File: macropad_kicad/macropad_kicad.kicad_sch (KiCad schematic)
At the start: 34 parts, among them J1 OLED_128x64, SW1 RotaryEncoder_Switch, SW2 RotaryEncoder_Switch, U1 MOUDLE-SEEEDUINO-XIAO

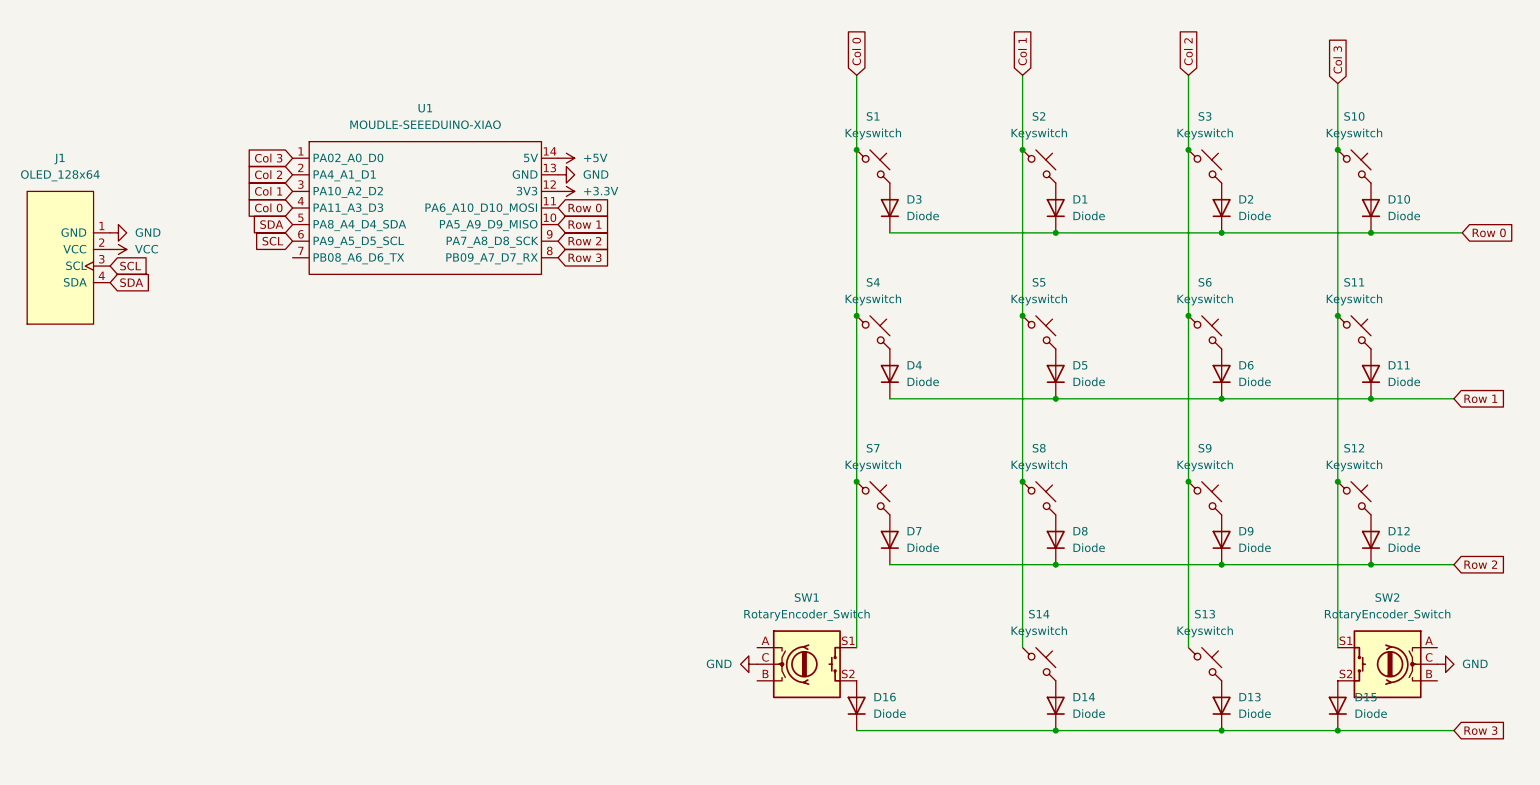
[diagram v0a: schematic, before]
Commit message: Add schematic for matrix and OLED display integration Re-Implemented schematic as there in not enough pins
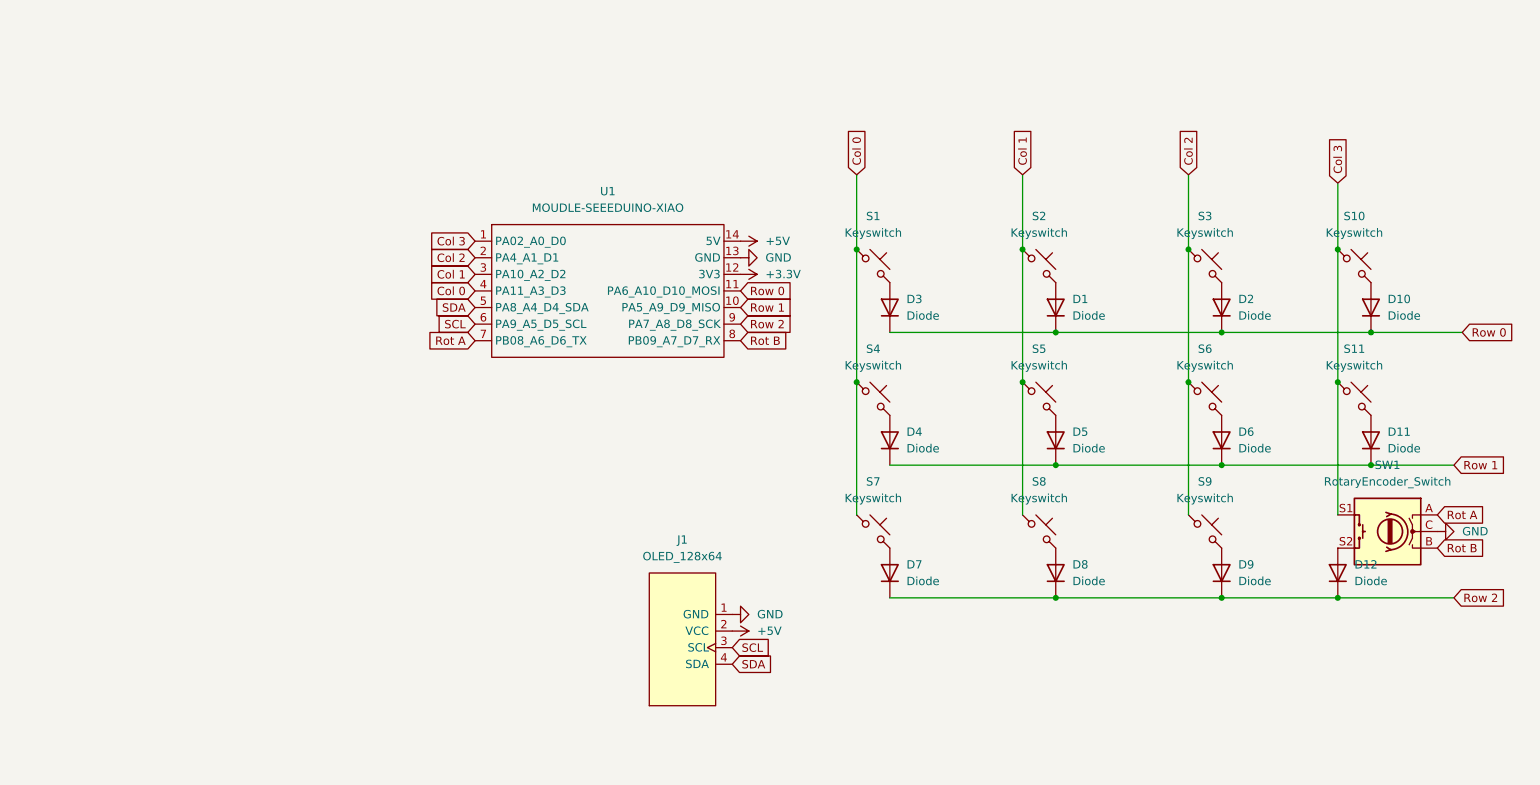
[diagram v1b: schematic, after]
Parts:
- removed D13, D14, D15, D16: Diode, symbol ScottoKeebs:Placeholder_Diode
- removed S12, S13, S14: Keyswitch, symbol ScottoKeebs:Placeholder_Keyswitch
- removed SW2: RotaryEncoder_Switch, symbol Device:RotaryEncoder_Switch
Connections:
- net Row 3 is gone; now on net Rot B: U1.8 (PB09_A7_D7_RX)
- net VCC is gone; now on net +5V: J1.2 (VCC)
- net Col 0: no longer SW1.S1
- net Col 3: now also SW1.S1
- net at D12.2 (A): now also SW1.S2
- net Rot A: now reaches U1.7 (PB08_A6_D6_TX)
- net Rot A: now also SW1.A
- net Rot B: now reaches SW1.B
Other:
- moved on the sheet: D1, D10, D11, D2, D3, D4, D5, D6, D7, D8, D9, J1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

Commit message: Update footprint properties and library URI in schematic files created pcb with footprints
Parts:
- D1, D10, D11, D12, D2, D3, D4, D5, D6, D7, D8, D9: footprint (none) -> ScottoKeebs_Components:Diode_DO-35
- S1, S10, S11, S2, S3, S4, S5, S6, S7, S8, S9: footprint (none) -> Button_Switch_Keyboard:SW_Cherry_MX_1.00u_PCB
- SW1: footprint (none) -> Rotary_Encoder:RotaryEncoder_Alps_EC11E-Switch_Vertical_H20mm
- U1: footprint (none) -> XIAO_PCB:MOUDLE14P-2.54-21X17.8MM
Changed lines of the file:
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@@
 			)
 		)
-		(property "Footprint" ""
+		(property "Footprint" "Button_Switch_Keyboard:SW_Cherry_MX_1.00u_PCB"
 			(at 180.34 121.92 0)
 			(effects
@@
 			)
 		)
-		(property "Footprint" ""
+		(property "Footprint" "ScottoKeebs_Components:Diode_DO-35"
 			(at 233.68 87.63 0)
 			(effects
@@
 			)
 		)
-		(property "Footprint" ""
+		(property "Footprint" "Button_Switch_Keyboard:SW_Cherry_MX_1.00u_PCB"
 			(at 231.14 81.28 0)
 			(effects
@@
 			)
 		)
-		(property "Footprint" ""
+		(property "Footprint" "Button_Switch_Keyboard:SW_Cherry_MX_1.00u_PCB"
 			(at 205.74 121.92 0)
 			(effects
@@
 			)
 		)
-		(property "Footprint" ""
+		(property "Footprint" "ScottoKeebs_Components:Diode_DO-35"
 			(at 208.28 87.63 0)
 			(effects
@@
 			)
 		)
-		(property "Footprint" ""
+		(property "Footprint" "ScottoKeebs_Components:Diode_DO-35"
 			(at 233.68 128.27 0)
 			(effects
@@
 			)
 		)
-		(property "Footprint" ""
+		(property "Footprint" "Button_Switch_Keyboard:SW_Cherry_MX_1.00u_PCB"
 			(at 180.34 81.28 0)
 			(effects
@@
 			)
 		)
-		(property "Footprint" ""
+		(property "Footprint" "ScottoKeebs_Components:Diode_DO-35"
 			(at 233.68 107.95 0)
 			(effects
@@
 			)
 		)
-		(property "Footprint" ""
+		(property "Footprint" "Button_Switch_Keyboard:SW_Cherry_MX_1.00u_PCB"
 			(at 205.74 101.6 0)
 			(effects
@@
 			)
 		)
-		(property "Footprint" ""
+		(property "Footprint" "ScottoKeebs_Components:Diode_DO-35"
 			(at 208.28 107.95 0)
 			(effects
@@
 			)
 		)
-		(property "Footprint" ""
+		(property "Footprint" "ScottoKeebs_Components:Diode_DO-35"
 			(at 208.28 128.27 0)
 			(effects
@@
 			)
 		)
-		(property "Footprint" ""
+		(property "Footprint" "ScottoKeebs_Components:Diode_DO-35"
 			(at 256.54 87.63 0)
 			(effects
@@
 			)
 		)
-		(property "Footprint" ""
+		(property "Footprint" "XIAO_PCB:MOUDLE14P-2.54-21X17.8MM"
 			(at 121.92 82.55 0)
 			(effects
@@
 			)
 		)
-		(property "Footprint" ""
+		(property "Footprint" "Button_Switch_Keyboard:SW_Cherry_MX_1.00u_PCB"
 			(at 205.74 81.28 0)
 			(effects
@@
 			)
 		)
-		(property "Footprint" ""
+		(property "Footprint" "ScottoKeebs_Components:Diode_DO-35"
 			(at 182.88 107.95 0)
 			(effects
@@
 			)
 		)
-		(property "Footprint" ""
+		(property "Footprint" "Rotary_Encoder:RotaryEncoder_Alps_EC11E-Switch_Vertical_H20mm"
 			(at 262.89 117.856 0)
 			(effects
@@
 			)
 		)
-		(property "Footprint" ""
+		(property "Footprint" "ScottoKeebs_Components:Diode_DO-35"
 			(at 256.54 107.95 0)
 			(effects
@@
 			)
 		)
-		(property "Footprint" ""
+		(property "Footprint" "Button_Switch_Keyboard:SW_Cherry_MX_1.00u_PCB"
 			(at 254 81.28 0)
 			(effects
@@
 			)
 		)
-		(property "Footprint" ""
+		(property "Footprint" "ScottoKeebs_Components:Diode_DO-35"
 			(at 251.46 128.27 0)
 			(effects
@@
 			)
 		)
-		(property "Footprint" ""
+		(property "Footprint" "Button_Switch_Keyboard:SW_Cherry_MX_1.00u_PCB"
 			(at 180.34 101.6 0)
 			(effects
@@
 			)
 		)
-		(property "Footprint" ""
+		(property "Footprint" "ScottoKeebs_Components:Diode_DO-35"
 			(at 182.88 128.27 0)
 			(effects
@@
 			)
 		)
-		(property "Footprint" ""
+		(property "Footprint" "Button_Switch_Keyboard:SW_Cherry_MX_1.00u_PCB"
 			(at 254 101.6 0)
 			(effects
@@
 			)
 		)
-		(property "Footprint" ""
+		(property "Footprint" "Button_Switch_Keyboard:SW_Cherry_MX_1.00u_PCB"
 			(at 231.14 101.6 0)
 			(effects
@@
 			)
 		)
-		(property "Footprint" ""
+		(property "Footprint" "ScottoKeebs_Components:Diode_DO-35"
 			(at 182.88 87.63 0)
 			(effects
@@
 			)
 		)
-		(property "Footprint" ""
+		(property "Footprint" "Button_Switch_Keyboard:SW_Cherry_MX_1.00u_PCB"
 			(at 231.14 121.92 0)
 			(effects

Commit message: fixed scheme
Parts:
- S1, S10, S11, S2, S3, S4, S5, S6, S7, S8, S9: footprint Button_Switch_Keyboard:SW_Cherry_MX_1.00u_PCB -> ScottoKeebs_MX:MX_PCB_1.00u
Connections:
- net Col 0: now also S5.1, S9.1; no longer S4.1, S7.1
- net Col 1: now also S10.1, S6.1; no longer S5.1, S8.1
- net Col 2: now also S11.1, S7.1; no longer S6.1, S9.1
- net Col 3: now also S4.1, S8.1; no longer S10.1, S11.1
- net Row 0: now also D4.1 (K); no longer D10.1 (K)
- net Row 1: now also D7.1 (K), D8.1 (K); no longer D11.1 (K), D4.1 (K)
- net Row 2: now also D10.1 (K), D11.1 (K); no longer D7.1 (K), D8.1 (K)
- net at D2.2 (A): now also S2.2; no longer S3.2
- net at D1.2 (A): now also S1.2; no longer S2.2
- net at D3.2 (A): now also S3.2; no longer S1.2
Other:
- moved on the sheet: D1, D10, D11, D2, D3, D4, D5, D6, D7, D8, D9, J1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

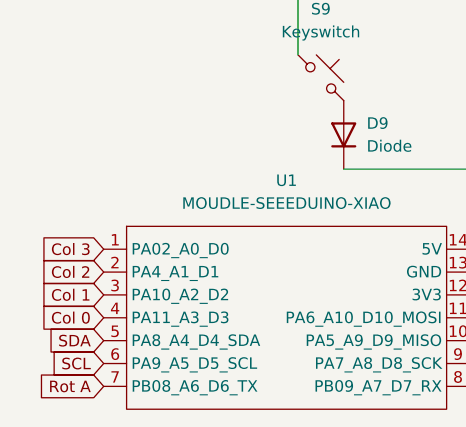
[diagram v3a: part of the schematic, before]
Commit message: routed all wires manually
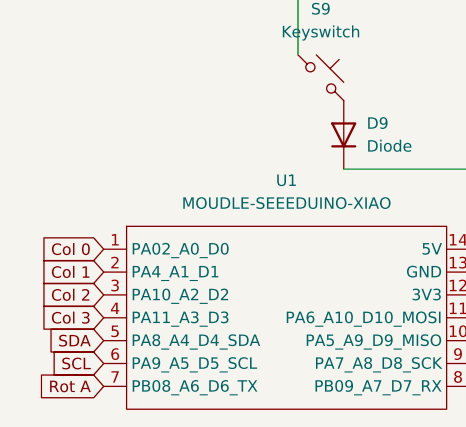
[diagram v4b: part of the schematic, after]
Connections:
- net Col 0: now also U1.1 (PA02_A0_D0); no longer U1.4 (PA11_A3_D3)
- net Col 1: now also U1.2 (PA4_A1_D1); no longer U1.3 (PA10_A2_D2)
- net Col 2: now also U1.3 (PA10_A2_D2); no longer U1.2 (PA4_A1_D1)
- net Col 3: now also U1.4 (PA11_A3_D3); no longer U1.1 (PA02_A0_D0)
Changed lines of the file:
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@@
 	(global_label "Col 2"
 		(shape input)
-		(at 156.21 143.51 180)
+		(at 156.21 146.05 180)
 		(fields_autoplaced yes)
 		(effects
@@
 		)
 		(property "Intersheetrefs" "${INTERSHEET_REFS}"
-			(at 147.9635 143.51 0)
+			(at 147.9635 146.05 0)
 			(effects
 				(font
@@
 	(global_label "Col 1"
 		(shape input)
-		(at 156.21 146.05 180)
+		(at 156.21 143.51 180)
 		(fields_autoplaced yes)
 		(effects
@@
 		)
 		(property "Intersheetrefs" "${INTERSHEET_REFS}"
-			(at 147.9635 146.05 0)
+			(at 147.9635 143.51 0)
 			(effects
 				(font
@@
 	)
 	(global_label "Col 0"
+		(shape input)
+		(at 156.21 140.97 180)
+		(fields_autoplaced yes)
+		(effects
+			(font
+				(size 1.27 1.27)
+			)
+			(justify right)
+		)
+		(property "Intersheetrefs" "${INTERSHEET_REFS}"
+			(at 147.9635 140.97 0)
+			(effects
+				(font
+					(size 1.27 1.27)
+				)
+				(justify right)
+				(hide yes)
+			)
+		)
+	)
+	(global_label "Col 3"
 		(shape input)
 		(at 156.21 148.59 180)
@@
 			(effects
 				(font
-					(size 1.27 1.27)
-				)
-				(justify right)
-				(hide yes)
-			)
-		)
-	)
-	(global_label "Col 3"
-		(shape input)
-		(at 156.21 140.97 180)
-		(fields_autoplaced yes)
-		(effects
-			(font
-				(size 1.27 1.27)
-			)
-			(justify right)
-		)
-		(property "Intersheetrefs" "${INTERSHEET_REFS}"
-			(at 147.9635 140.97 0)
-			(effects
-				(font
